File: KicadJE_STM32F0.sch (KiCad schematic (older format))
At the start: 101 parts, among them J401 CV1, J402 CV2, J403 OUT1, J404 OUT2, J405 OUT3, J406 OUT4, J407 IN1, J408 IN2, J409 I2C, P401 Doepfer_Power_16pin, SW401 SW_SPDT, U401 TL072, U402 TL072, U403 TL072, U404 TL072, U405 MCP4822

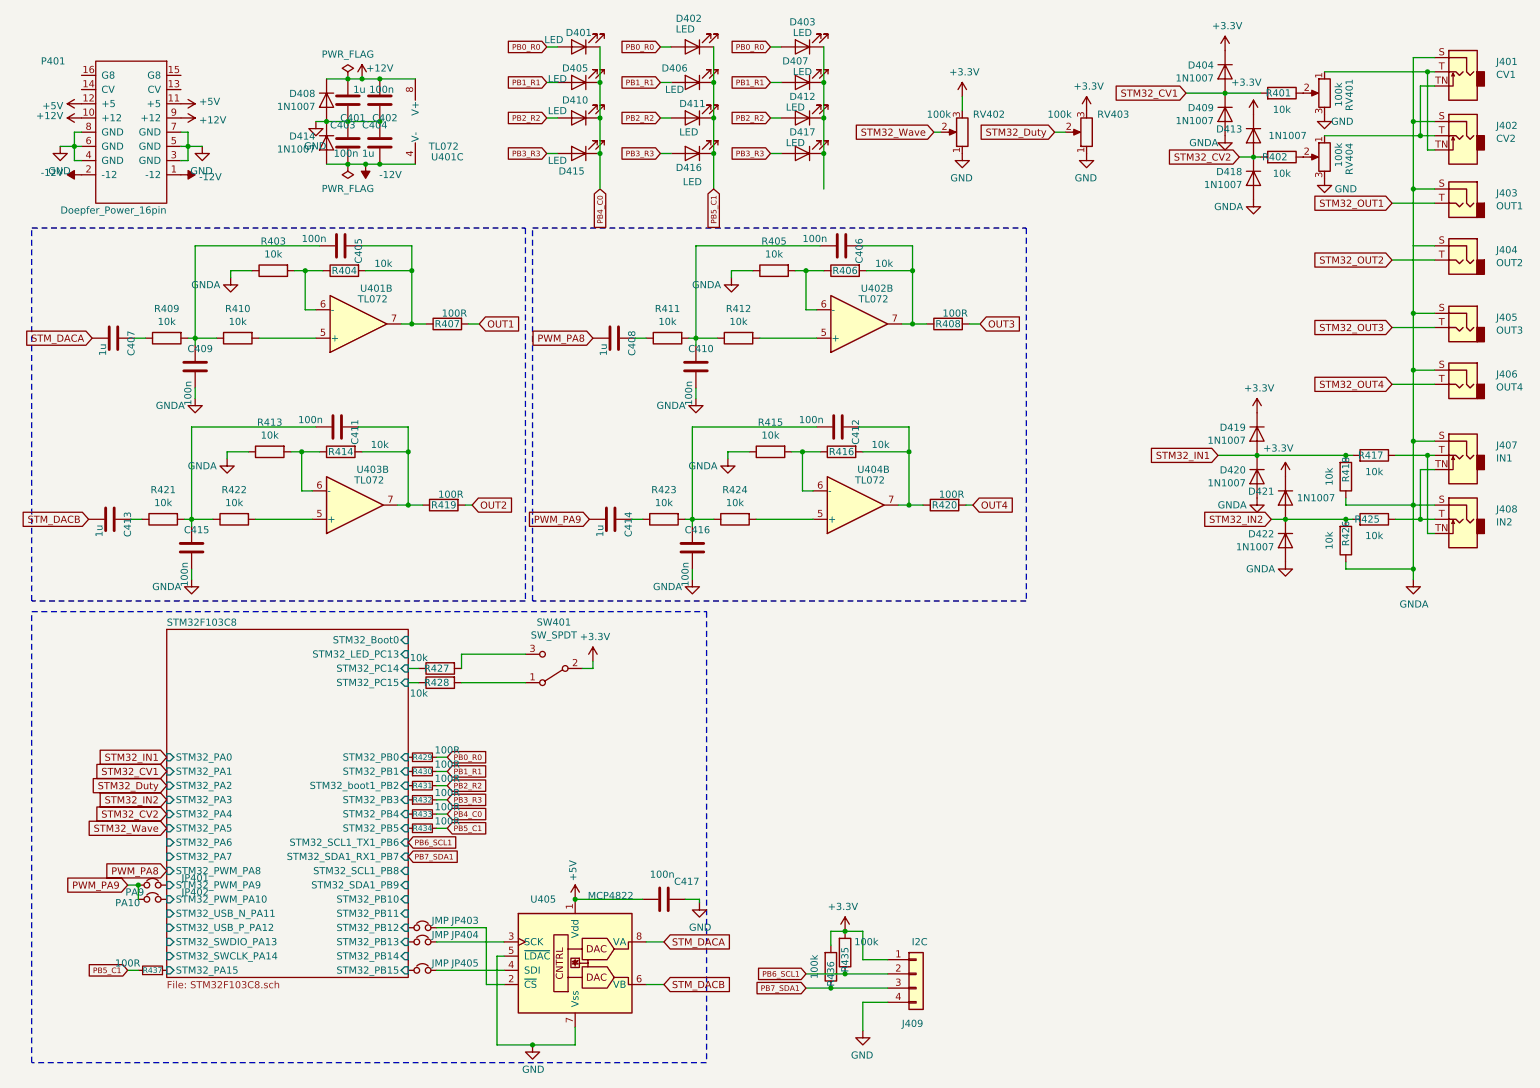
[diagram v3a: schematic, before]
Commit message: STM32 Initiated layout
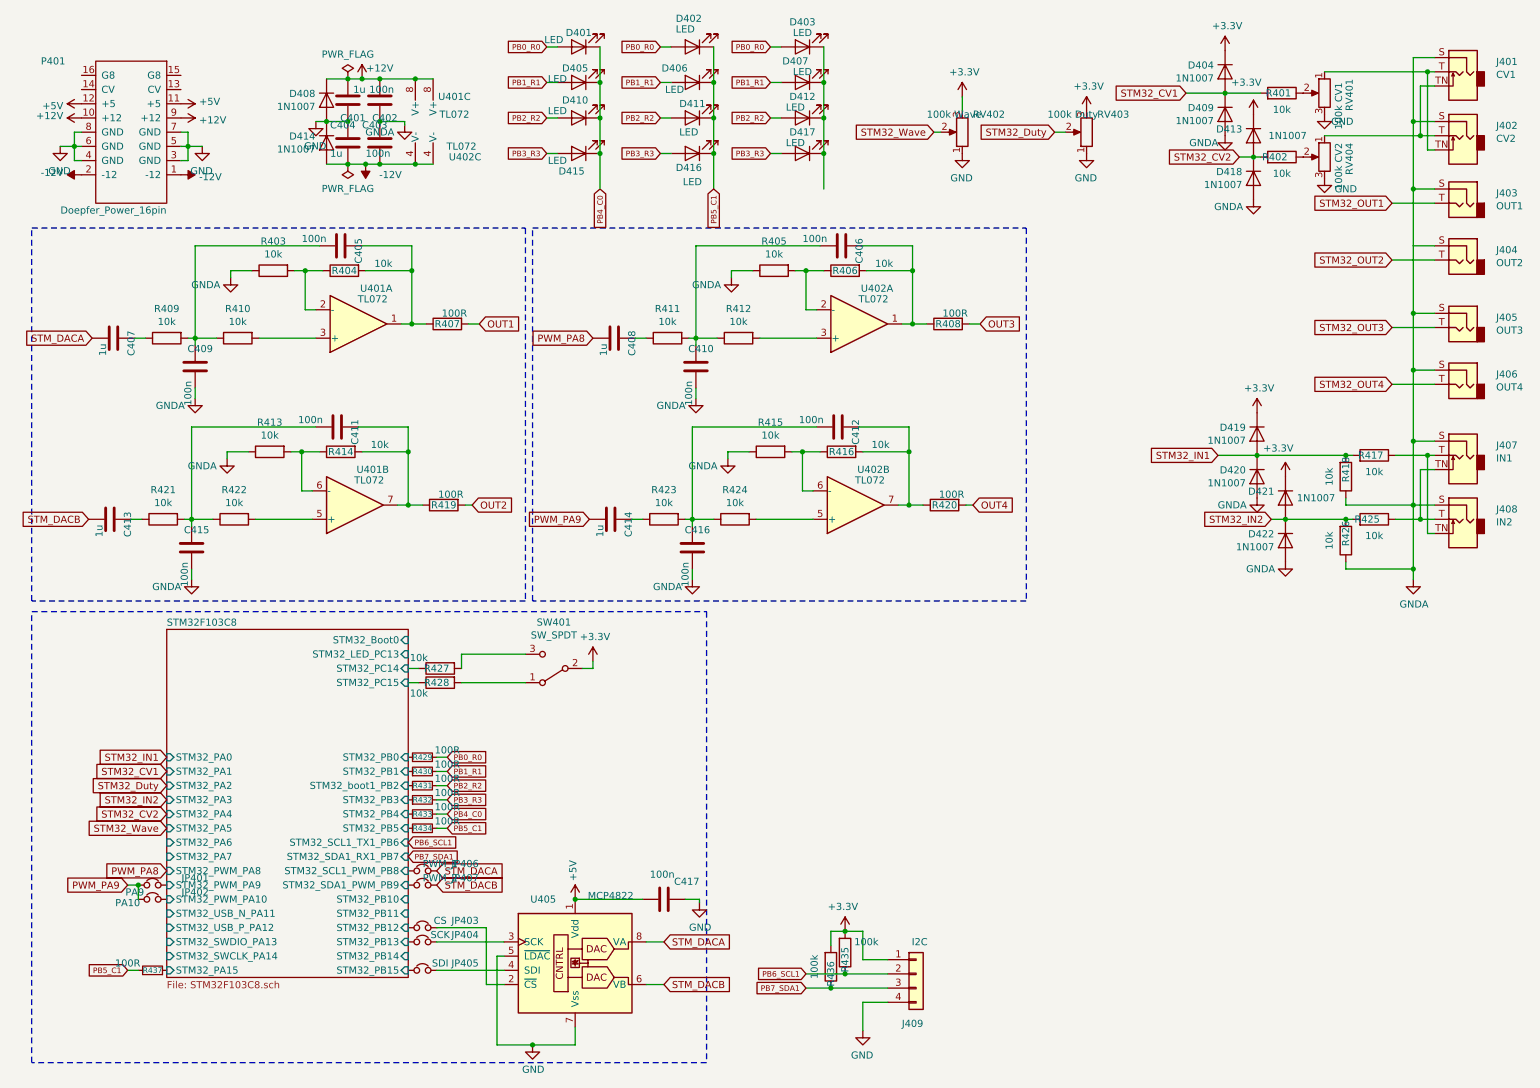
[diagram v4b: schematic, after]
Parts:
- added JP406: PWM_1, Connector_PinSocket_2.54mm:PinSocket_1x02_P2.54mm_Vertical, symbol Device:Jumper_NC_Small
- added JP407: PWM_2, Connector_PinSocket_2.54mm:PinSocket_1x02_P2.54mm_Vertical, symbol Device:Jumper_NC_Small
- added unit 3 of U402
- JP403: value JMP -> CS
- JP404: value JMP -> SCK
- JP405: value JMP -> SDI
- RV401: value 100k -> 100k CV1
- RV402: value 100k -> 100k Wave
- RV403: value 100k -> 100k Duty
- RV404: value 100k -> 100k CV2
- renumbered U403 to U401, U404 to U402
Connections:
- net +12V: now also U402.8 (V+)
- net -12V: now also U402.4 (V-)
- net GND: no longer C402.1, C403.1
- net GNDA: now also C402.1, C403.1
- net STM_DACA: now also JP406.1
- net STM_DACB: now also JP407.1
- net at R410.2: now also U401.3 (+); no longer U401.5 (+)
- net at R403.2, R404.1: now also U401.2 (-); no longer U401.6 (-)
- net at C405.1, R404.2, R407.1: now also U401.1; no longer U401.7
- net at R412.2: now also U402.3 (+); no longer U402.5 (+)
- net at R405.2, R406.1: now also U402.2 (-); no longer U402.6 (-)
- net at C406.1, R406.2, R408.1: now also U402.1; no longer U402.7
- new net STM32F103C8/STM32_SCL1_PWM_PB8: JP406.2
- new net STM32F103C8/STM32_SDA1_PWM_PB9: JP407.2
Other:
- moved on the sheet: C403, C404
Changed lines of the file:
@@
 AR Path="/5CE53731/5CE65671" Ref="RV403"  Part="1"
 F 0 "RV403" H 7950 1075 50  0000 R CNN
-F 1 "100k" H 8300 1075 50  0000 R CNN
+F 1 "100k Duty" H 8300 1075 50  0000 R CNN
 F 2 "Potentiometer_THT:Potentiometer_China_RK09_Single_Vertical_AJ" H 8025 1200 50  0001 C CNN
 F 3 "~" H 8025 1200 50  0001 C CNN
@@
 AR Path="/5CE53731/5CE65683" Ref="RV404"  Part="1"
 F 0 "RV404" V 9525 1475 50  0000 R CNN
-F 1 "100k" V 9600 1475 50  0000 R CNN
+F 1 "100k CV2" V 9600 1475 50  0000 R CNN
 F 2 "Potentiometer_THT:Potentiometer_China_RK09_Single_Vertical_AJ" H 9700 1375 50  0001 C CNN
 F 3 "~" H 9700 1375 50  0001 C CNN
@@
 AR Path="/5CE53731/5CE65690" Ref="RV401"  Part="1"
 F 0 "RV401" V 9525 1025 50  0000 R CNN
-F 1 "100k" V 9600 1000 50  0000 R CNN
+F 1 "100k CV1" V 9600 1000 50  0000 R CNN
 F 2 "Potentiometer_THT:Potentiometer_China_RK09_Single_Vertical_AJ" H 9700 925 50  0001 C CNN
 F 3 "~" H 9700 925 50  0001 C CNN
@@
 AR Path="/5CE53731/5CE6569C" Ref="RV402"  Part="1"
 F 0 "RV402" H 7075 1075 50  0000 R CNN
-F 1 "100k" H 7400 1075 50  0000 R CNN
+F 1 "100k Wave" H 7400 1075 50  0000 R CNN
 F 2 "Potentiometer_THT:Potentiometer_China_RK09_Single_Vertical_AJ" H 7150 1200 50  0001 C CNN
 F 3 "~" H 7150 1200 50  0001 C CNN
@@
 P 2875 3825
 AR Path="/5CE656C6" Ref="U?"  Part="2"
-AR Path="/5CE53731/5CE656C6" Ref="U403"  Part="2"
-F 0 "U403" H 3000 3575 50  0000 C CNN
+AR Path="/5CE53731/5CE656C6" Ref="U401"  Part="2"
+F 0 "U401" H 3000 3575 50  0000 C CNN
 F 1 "TL072" H 2975 3650 50  0000 C CNN
 F 2 "AJ:AJ_SO-8_5.3x6.2mm_P1.27mm" H 2875 3825 50  0001 C CNN
@@
 $Comp
 L Amplifier_Operational:TL072 U?
-U 2 1 5CE6572C
+U 1 1 5CE6572C
 P 2900 2550
 AR Path="/5CE6572C" Ref="U?"  Part="2"
-AR Path="/5CE53731/5CE6572C" Ref="U401"  Part="2"
+AR Path="/5CE53731/5CE6572C" Ref="U401"  Part="1"
 F 0 "U401" H 3025 2300 50  0000 C CNN
 F 1 "TL072" H 3000 2375 50  0000 C CNN
 F 2 "AJ:AJ_SO-8_5.3x6.2mm_P1.27mm" H 2900 2550 50  0001 C CNN
 F 3 "http://www.ti.com/lit/ds/symlink/tl071.pdf" H 2900 2550 50  0001 C CNN
-	2    2900 2550
+	1    2900 2550
 	1    0    0    1
 $EndComp
@@
 L Device:C C?
 U 1 1 5CE76D09
-P 2825 1275
+P 3050 1275
 AR Path="/5CE76D09" Ref="C?"  Part="1"
 AR Path="/5CD3F059/5CE76D09" Ref="C?"  Part="1"
 AR Path="/5CE53731/5CE76D09" Ref="C403"  Part="1"
-F 0 "C403" H 2700 1400 50  0000 L CNN
-F 1 "100n" H 2725 1200 50  0000 L CNN
-F 2 "Capacitor_SMD:C_0805_2012Metric_Pad1.15x1.40mm_HandSolder" H 2863 1125 50  0001 C CNN
+F 0 "C403" H 2925 1400 50  0000 L CNN
+F 1 "100n" H 2950 1200 50  0000 L CNN
+F 2 "Capacitor_SMD:C_0805_2012Metric_Pad1.15x1.40mm_HandSolder" H 3088 1125 50  0001 C CNN
+F 3 "~" H 3050 1275 50  0001 C CNN
+	1    3050 1275
+	1    0    0    -1
+$EndComp
+$Comp
+L Device:C C?
+U 1 1 5CE76D0F
+P 2825 1275
+AR Path="/5CE76D0F" Ref="C?"  Part="1"
+AR Path="/5CD3F059/5CE76D0F" Ref="C?"  Part="1"
+AR Path="/5CE53731/5CE76D0F" Ref="C404"  Part="1"
+F 0 "C404" H 2700 1400 50  0000 L CNN
+F 1 "1u" H 2700 1200 50  0000 L CNN
+F 2 "Capacitor_SMD:C_1206_3216Metric_Pad1.42x1.75mm_HandSolder" H 2863 1125 50  0001 C CNN
 F 3 "~" H 2825 1275 50  0001 C CNN
 	1    2825 1275
 	1    0    0    -1
 $EndComp
-$Comp
-L Device:C C?
-U 1 1 5CE76D0F
-P 3050 1275
-AR Path="/5CE76D0F" Ref="C?"  Part="1"
-AR Path="/5CD3F059/5CE76D0F" Ref="C?"  Part="1"
-AR Path="/5CE53731/5CE76D0F" Ref="C404"  Part="1"
-F 0 "C404" H 2925 1400 50  0000 L CNN
-F 1 "1u" H 2925 1200 50  0000 L CNN
-F 2 "Capacitor_SMD:C_1206_3216Metric_Pad1.42x1.75mm_HandSolder" H 3088 1125 50  0001 C CNN
-F 3 "~" H 3050 1275 50  0001 C CNN
-	1    3050 1275
-	1    0    0    -1
-$EndComp
-Connection ~ 3050 1125
-Wire Wire Line
-	3050 1125 2825 1125
 Wire Wire Line
 	3050 1425 2950 1425
@@
 AR Path="/5CE76D40" Ref="U?"  Part="3"
 AR Path="/5CE53731/5CE76D40" Ref="U401"  Part="3"
-F 0 "U401" H 3525 875 50  0000 C CNN
-F 1 "TL072" H 3500 950 50  0000 C CNN
+F 0 "U401" H 3575 1300 50  0000 C CNN
+F 1 "TL072" H 3575 1175 50  0000 C CNN
 F 2 "" H 3400 1125 50  0001 C CNN
 F 3 "http://www.ti.com/lit/ds/symlink/tl071.pdf" H 3400 1125 50  0001 C CNN
@@
 AR Path="/5CE53731/5CE93C4D" Ref="JP405"  Part="1"
 F 0 "JP405" H 3050 7150 50  0000 C CNN
-F 1 "JMP" H 3225 7150 50  0000 C CNN
+F 1 "SDI" H 3225 7150 50  0000 C CNN
 F 2 "Connector_PinSocket_2.54mm:PinSocket_1x02_P2.54mm_Vertical" H 3350 7100 50  0001 C CNN
 F 3 "~" H 3350 7100 50  0001 C CNN
@@
 AR Path="/5CE53731/5CE93C53" Ref="JP404"  Part="1"
 F 0 "JP404" H 3050 6950 50  0000 C CNN
-F 1 "JMP" H 3225 6950 50  0000 C CNN
+F 1 "SCK" H 3225 6950 50  0000 C CNN
 F 2 "Connector_PinSocket_2.54mm:PinSocket_1x02_P2.54mm_Vertical" H 3350 6900 50  0001 C CNN
 F 3 "~" H 3350 6900 50  0001 C CNN
@@
 AR Path="/5CE53731/5CE93C59" Ref="JP403"  Part="1"
 F 0 "JP403" H 3050 6850 50  0000 C CNN
-F 1 "JMP" H 3225 6850 50  0000 C CNN
+F 1 "CS" H 3225 6850 50  0000 C CNN
 F 2 "Connector_PinSocket_2.54mm:PinSocket_1x02_P2.54mm_Vertical" H 3350 6800 50  0001 C CNN
 F 3 "~" H 3350 6800 50  0001 C CNN
@@
 F28 "STM32_LED_PC13" I R 3250 4875 50
 F29 "STM32_boot1_PB2" I R 3250 5800 50
-F30 "STM32_SDA1_PB9" I R 3250 6500 50
-F31 "STM32_SCL1_PB8" I R 3250 6400 50
-F32 "STM32_SDA1_RX1_PB7" I R 3250 6300 50
-F33 "STM32_SCL1_TX1_PB6" I R 3250 6200 50
-F34 "STM32_USB_P_PA12" I L 1550 6800 50
-F35 "STM32_PWM_PA8" I L 1550 6400 50
-F36 "STM32_PWM_PA9" I L 1550 6500 50
-F37 "STM32_PWM_PA10" I L 1550 6600 50
+F30 "STM32_SDA1_RX1_PB7" I R 3250 6300 50
+F31 "STM32_SCL1_TX1_PB6" I R 3250 6200 50
+F32 "STM32_USB_P_PA12" I L 1550 6800 50
+F33 "STM32_PWM_PA8" I L 1550 6400 50
+F34 "STM32_PWM_PA9" I L 1550 6500 50
+F35 "STM32_PWM_PA10" I L 1550 6600 50
+F36 "STM32_SDA1_PWM_PB9" I R 3250 6500 50
+F37 "STM32_SCL1_PWM_PB8" I R 3250 6400 50
 $EndSheet
 Wire Wire Line
@@
 P 6400 3825
 AR Path="/5CF59152" Ref="U?"  Part="2"
-AR Path="/5CE53731/5CF59152" Ref="U404"  Part="2"
-F 0 "U404" H 6525 3575 50  0000 C CNN
+AR Path="/5CE53731/5CF59152" Ref="U402"  Part="2"
+F 0 "U402" H 6525 3575 50  0000 C CNN
 F 1 "TL072" H 6500 3650 50  0000 C CNN
 F 2 "AJ:AJ_SO-8_5.3x6.2mm_P1.27mm" H 6400 3825 50  0001 C CNN
@@
 $Comp
 L Amplifier_Operational:TL072 U?
-U 2 1 5CF591DE
+U 1 1 5CF591DE
 P 6425 2550
 AR Path="/5CF591DE" Ref="U?"  Part="2"
-AR Path="/5CE53731/5CF591DE" Ref="U402"  Part="2"
+AR Path="/5CE53731/5CF591DE" Ref="U402"  Part="1"
 F 0 "U402" H 6550 2300 50  0000 C CNN
 F 1 "TL072" H 6525 2375 50  0000 C CNN
 F 2 "AJ:AJ_SO-8_5.3x6.2mm_P1.27mm" H 6425 2550 50  0001 C CNN
 F 3 "http://www.ti.com/lit/ds/symlink/tl071.pdf" H 6425 2550 50  0001 C CNN
-	2    6425 2550
+	1    6425 2550
 	1    0    0    1
 $EndComp
@@
 Wire Wire Line
 	2675 825  2825 825
+$Comp
+L power:GNDA #PWR?
+U 1 1 5D54D317
+P 3225 1150
+AR Path="/5D54D317" Ref="#PWR?"  Part="1"
+AR Path="/5CD3F059/5D54D317" Ref="#PWR?"  Part="1"
+AR Path="/5CE53731/5D54D317" Ref="#PWR0441"  Part="1"
+F 0 "#PWR0441" H 3225 900 50  0001 C CNN
+F 1 "GNDA" H 3400 1100 50  0000 C CNN
+F 2 "" H 3225 1150 50  0001 C CNN
+F 3 "" H 3225 1150 50  0001 C CNN
+	1    3225 1150
+	-1   0    0    -1
+$EndComp
+Wire Wire Line
+	3050 1125 3225 1125
+Wire Wire Line
+	3225 1125 3225 1150
+Connection ~ 3050 1125
+$Comp
+L Device:Jumper_NC_Small JP?
+U 1 1 5D5634C3
+P 3350 6400
+AR Path="/5CE3E7A9/5D5634C3" Ref="JP?"  Part="1"
+AR Path="/5CE53731/5D5634C3" Ref="JP406"  Part="1"
+F 0 "JP406" H 3050 6450 50  0000 C CNN
+F 1 "PWM_1" H 3225 6450 50  0000 C CNN
+F 2 "Connector_PinSocket_2.54mm:PinSocket_1x02_P2.54mm_Vertical" H 3350 6400 50  0001 C CNN
+F 3 "~" H 3350 6400 50  0001 C CNN
+	1    3350 6400
+	-1   0    0    -1
+$EndComp
+$Comp
+L Device:Jumper_NC_Small JP?
+U 1 1 5D563A96
+P 3350 6500
+AR Path="/5CE3E7A9/5D563A96" Ref="JP?"  Part="1"
+AR Path="/5CE53731/5D563A96" Ref="JP407"  Part="1"
+F 0 "JP407" H 3050 6550 50  0000 C CNN
+F 1 "PWM_2" H 3225 6550 50  0000 C CNN
+F 2 "Connector_PinSocket_2.54mm:PinSocket_1x02_P2.54mm_Vertical" H 3350 6500 50  0001 C CNN
+F 3 "~" H 3350 6500 50  0001 C CNN
+	1    3350 6500
+	-1   0    0    -1
+$EndComp
+Text GLabel 3450 6400 2    50   Input ~ 0
+STM_DACA
+Text GLabel 3450 6500 2    50   Input ~ 0
+STM_DACB
+$Comp
+L Amplifier_Operational:TL072 U?
+U 3 1 5D5708B8
+P 3525 1125
+AR Path="/5D5708B8" Ref="U?"  Part="3"
+AR Path="/5CE53731/5D5708B8" Ref="U402"  Part="3"
+F 0 "U402" H 3650 875 50  0000 C CNN
+F 1 "TL072" H 3625 950 50  0000 C CNN
+F 2 "" H 3525 1125 50  0001 C CNN
+F 3 "http://www.ti.com/lit/ds/symlink/tl071.pdf" H 3525 1125 50  0001 C CNN
+	3    3525 1125
+	1    0    0    -1
+$EndComp
+Wire Wire Line
+	3300 1425 3425 1425
+Connection ~ 3300 1425
+Wire Wire Line
+	3300 825  3425 825
+Connection ~ 3300 825
 $EndSCHEMATC

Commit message: Changed Op Amp A and B
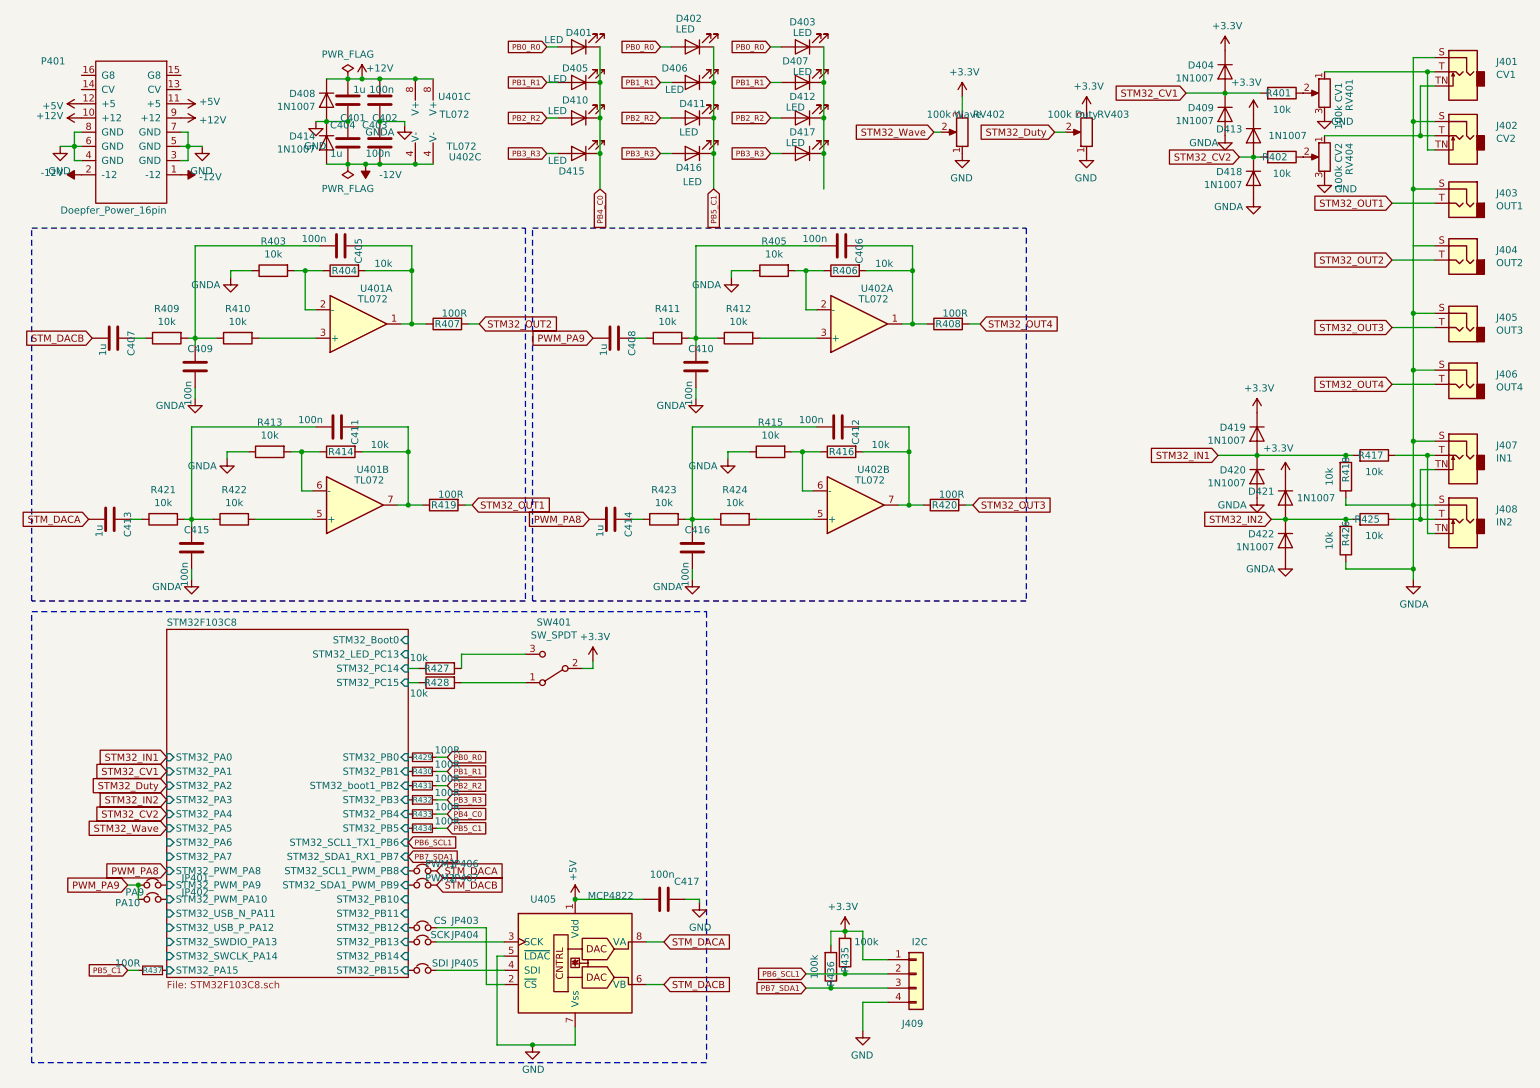
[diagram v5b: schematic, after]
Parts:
- JP406: value PWM_1 -> PWM1
- JP407: value PWM_2 -> PWM2
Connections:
- net OUT1 is gone; now on net STM32_OUT2: R407.2
- net OUT2 is gone; now on net STM32_OUT1: R419.2
- net OUT3 is gone; now on net STM32_OUT4: R408.2
- net OUT4 is gone; now on net STM32_OUT3: R420.2
- net PWM_PA8: now also C414.2; no longer C408.2
- net PWM_PA9: now also C408.2; no longer C414.2
- net STM_DACA: now also C413.2; no longer C407.2
- net STM_DACB: now also C407.2; no longer C413.2
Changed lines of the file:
@@
 Connection ~ 10325 3825
 Connection ~ 10325 3375
+Text GLabel 3700 3825 2    50   Input ~ 0
+STM32_OUT1
 Text GLabel 3750 2550 2    50   Input ~ 0
-OUT1
-Text GLabel 3700 3825 2    50   Input ~ 0
-OUT2
+STM32_OUT2
 Wire Wire Line
 	3700 3825 3650 3825
@@
 Wire Wire Line
 	6100 3925 5700 3925
+Text GLabel 4550 2650 0    50   Input ~ 0
+PWM_PA9
 Text GLabel 4525 3925 0    50   Input ~ 0
-PWM_PA9
-Text GLabel 4550 2650 0    50   Input ~ 0
 PWM_PA8
 Connection ~ 5250 3925
@@
 	0    -1   1    0
 $EndComp
+Text GLabel 7225 3825 2    50   Input ~ 0
+STM32_OUT3
 Text GLabel 7275 2550 2    50   Input ~ 0
-OUT3
-Text GLabel 7225 3825 2    50   Input ~ 0
-OUT4
+STM32_OUT4
 Wire Wire Line
 	7225 3825 7175 3825
@@
 	6050 7225 6225 7225
 Connection ~ 6225 7225
+Text GLabel 1025 2650 0    50   Input ~ 0
+STM_DACB
 Text GLabel 1000 3925 0    50   Input ~ 0
-STM_DACB
-Text GLabel 1025 2650 0    50   Input ~ 0
 STM_DACA
 $Comp
@@
 AR Path="/5CE53731/5D5634C3" Ref="JP406"  Part="1"
 F 0 "JP406" H 3050 6450 50  0000 C CNN
-F 1 "PWM_1" H 3225 6450 50  0000 C CNN
+F 1 "PWM1" H 3225 6450 50  0000 C CNN
 F 2 "Connector_PinSocket_2.54mm:PinSocket_1x02_P2.54mm_Vertical" H 3350 6400 50  0001 C CNN
 F 3 "~" H 3350 6400 50  0001 C CNN
@@
 AR Path="/5CE53731/5D563A96" Ref="JP407"  Part="1"
 F 0 "JP407" H 3050 6550 50  0000 C CNN
-F 1 "PWM_2" H 3225 6550 50  0000 C CNN
+F 1 "PWM2" H 3225 6550 50  0000 C CNN
 F 2 "Connector_PinSocket_2.54mm:PinSocket_1x02_P2.54mm_Vertical" H 3350 6500 50  0001 C CNN
 F 3 "~" H 3350 6500 50  0001 C CNN
